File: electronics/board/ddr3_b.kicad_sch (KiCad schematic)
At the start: 22 parts, among them U2 DDR3-78

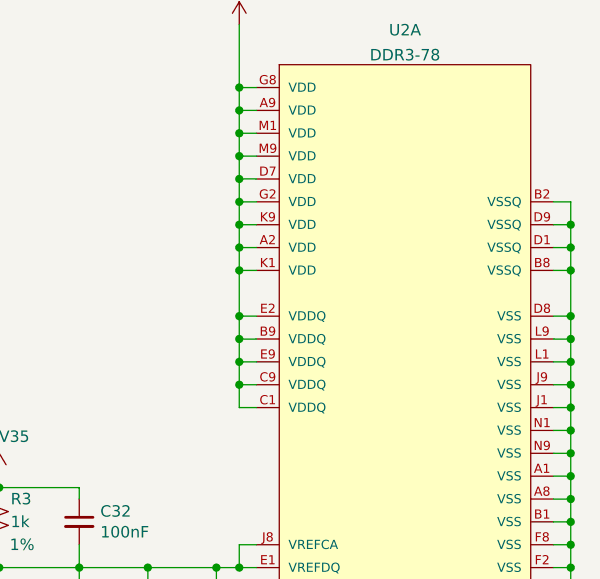
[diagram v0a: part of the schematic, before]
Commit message: Added gitignore, fixed the part
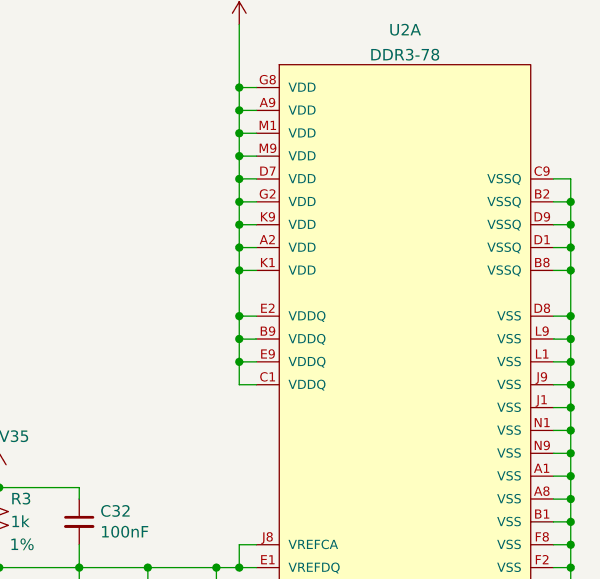
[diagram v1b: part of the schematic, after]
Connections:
- net +1V35: no longer U2.C9 (VDDQ)
- net GND: now also U2.C9 (VSSQ)
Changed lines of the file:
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@@
   (junction (at 222.25 105.41) (diameter 0) (color 0 0 0 0)
   )
-  (junction (at 185.42 102.87) (diameter 0) (color 0 0 0 0)
-  )
   (junction (at 222.25 100.33) (diameter 0) (color 0 0 0 0)
   )
@@
   (junction (at 222.25 102.87) (diameter 0) (color 0 0 0 0)
   )
+  (junction (at 222.25 82.55) (diameter 0) (color 0 0 0 0)
+  )
   (junction (at 144.145 40.005) (diameter 0) (color 0 0 0 0)
   )
@@
     (stroke (width 0) (type default) (color 0 0 0 0))
   )
+  (wire (pts (xy 222.25 80.01) (xy 222.25 82.55))
+    (stroke (width 0) (type default) (color 0 0 0 0))
+  )
   (wire (pts (xy 149.225 57.785) (xy 149.225 55.245))
     (stroke (width 0) (type default) (color 0 0 0 0))
@@
     (stroke (width 0) (type default) (color 0 0 0 0))
   )
+  (wire (pts (xy 220.345 80.01) (xy 222.25 80.01))
+    (stroke (width 0) (type default) (color 0 0 0 0))
+  )
   (wire (pts (xy 154.305 26.035) (xy 159.385 26.035))
     (stroke (width 0) (type default) (color 0 0 0 0))
@@
     (stroke (width 0) (type default) (color 0 0 0 0))
   )
-  (wire (pts (xy 185.42 102.87) (xy 185.42 105.41))
-    (stroke (width 0) (type default) (color 0 0 0 0))
-  )
   (bus (pts (xy 57.15 72.39) (xy 57.15 74.93))
-    (stroke (width 0) (type default) (color 0 0 0 0))
-  )
-  (wire (pts (xy 187.325 105.41) (xy 185.42 105.41))
     (stroke (width 0) (type default) (color 0 0 0 0))
   )
@@
   (symbol (lib_id "power:+1V35") (at 149.225 23.495 0) (unit 1)
     (in_bom yes) (on_board yes)
-    (property "Reference" "#PWR09" (id 0) (at 149.225 27.305 0)
+    (property "Reference" "#PWR0105" (id 0) (at 149.225 27.305 0)
       (effects (font (size 1.27 1.27)) hide)
     )
@@
   (symbol (lib_id "power:GND") (at 158.75 133.35 0) (unit 1)
     (in_bom yes) (on_board yes)
-    (property "Reference" "#PWR014" (id 0) (at 158.75 139.7 0)
+    (property "Reference" "#PWR0102" (id 0) (at 158.75 139.7 0)
       (effects (font (size 1.27 1.27)) hide)
     )
@@
   (symbol (lib_id "power:+1V35") (at 158.75 113.03 0) (unit 1)
     (in_bom yes) (on_board yes)
-    (property "Reference" "#PWR013" (id 0) (at 158.75 116.84 0)
+    (property "Reference" "#PWR0103" (id 0) (at 158.75 116.84 0)
       (effects (font (size 1.27 1.27)) hide)
     )
@@
   (symbol (lib_id "power:GND") (at 149.225 74.295 0) (unit 1)
     (in_bom yes) (on_board yes)
-    (property "Reference" "#PWR012" (id 0) (at 149.225 80.645 0)
+    (property "Reference" "#PWR0108" (id 0) (at 149.225 80.645 0)
       (effects (font (size 1.27 1.27)) hide)
     )
@@
   (symbol (lib_id "power:GND") (at 149.225 42.545 0) (unit 1)
     (in_bom yes) (on_board yes)
-    (property "Reference" "#PWR010" (id 0) (at 149.225 48.895 0)
+    (property "Reference" "#PWR0107" (id 0) (at 149.225 48.895 0)
       (effects (font (size 1.27 1.27)) hide)
     )
@@
   (symbol (lib_id "power:+1V35") (at 149.225 55.245 0) (unit 1)
     (in_bom yes) (on_board yes)
-    (property "Reference" "#PWR011" (id 0) (at 149.225 59.055 0)
+    (property "Reference" "#PWR0106" (id 0) (at 149.225 59.055 0)
       (effects (font (size 1.27 1.27)) hide)
     )
@@
   (symbol (lib_id "power:+1V35") (at 185.42 62.865 0) (unit 1)
     (in_bom yes) (on_board yes) (fields_autoplaced)
-    (property "Reference" "#PWR015" (id 0) (at 185.42 66.675 0)
+    (property "Reference" "#PWR0104" (id 0) (at 185.42 66.675 0)
       (effects (font (size 1.27 1.27)) hide)
     )
@@
   (symbol (lib_id "power:GND") (at 222.25 130.175 0) (unit 1)
     (in_bom yes) (on_board yes) (fields_autoplaced)
-    (property "Reference" "#PWR016" (id 0) (at 222.25 136.525 0)
-      (effects (font (size 1.27 1.27)) hide)
-    )
+    (property "Reference" "#PWR0101" (id 0) (at 222.25 136.525 0)
+      (effects (font (size 1.27 1.27)) hide)
+    )
